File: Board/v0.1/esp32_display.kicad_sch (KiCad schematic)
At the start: 7 parts, among them J1 USB_B_Micro

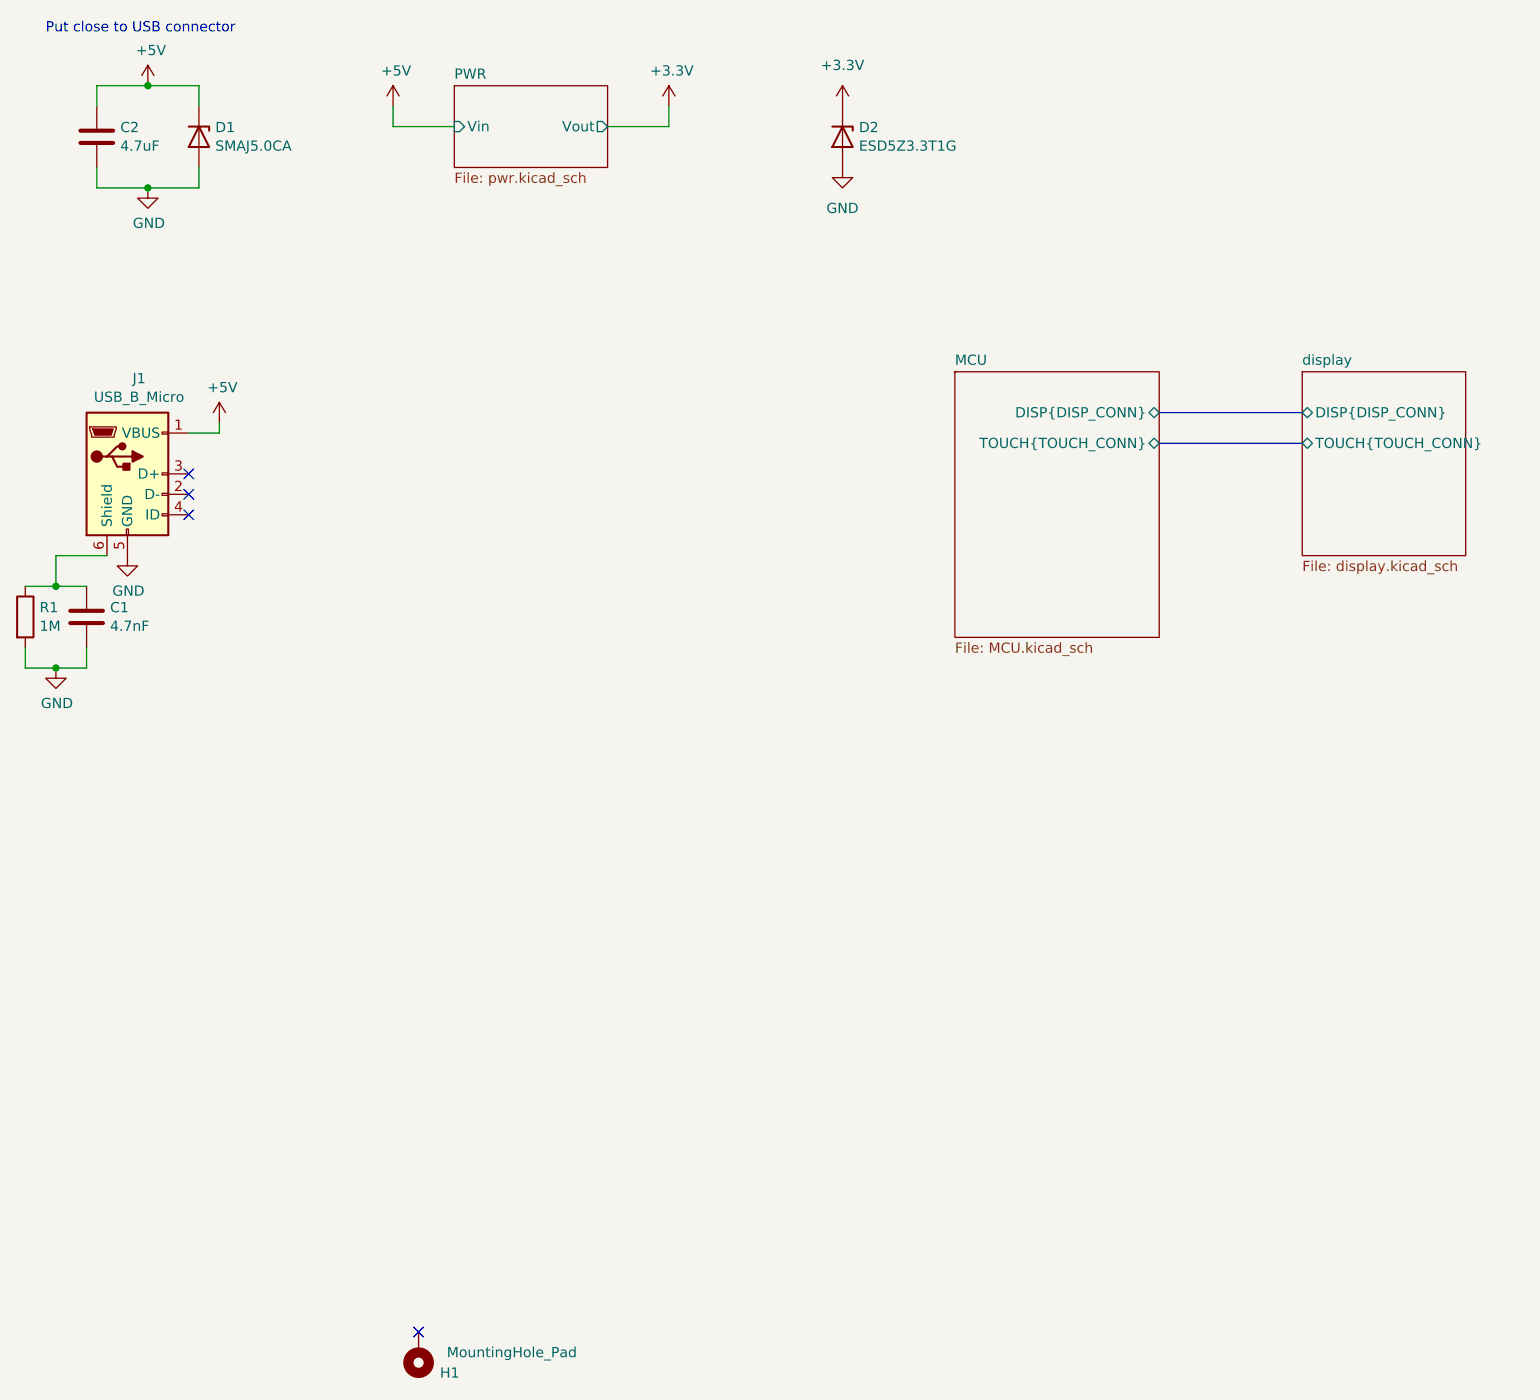
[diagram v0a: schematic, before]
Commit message: Clean schematics (add date and revision...)
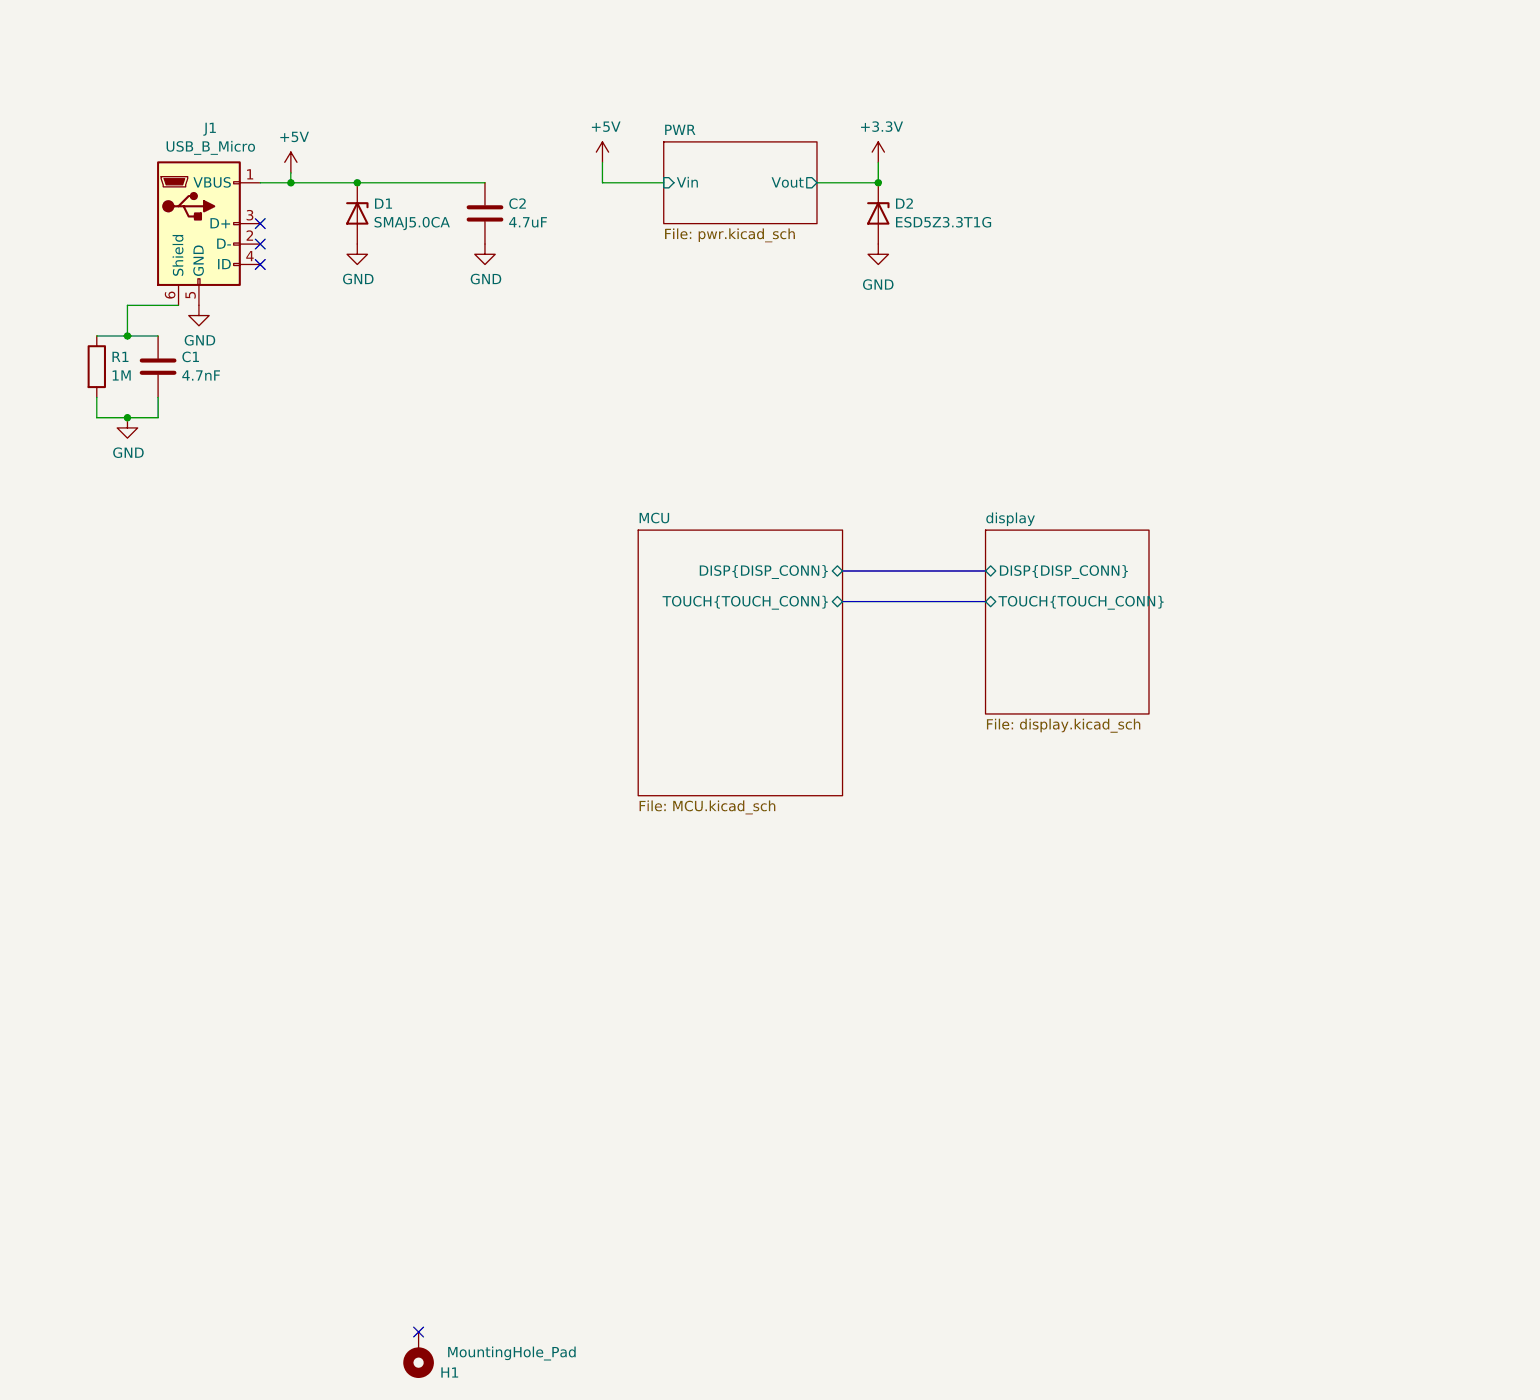
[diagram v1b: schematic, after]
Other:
- note removed: "Put close to USB connector"
- company: (none) -> Bzgec
- title: (none) -> ESP32_display
- moved on the sheet: C1, D2, J1, R1

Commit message: Add polyfuse, 3.3V status LED, USB_CONN sheet
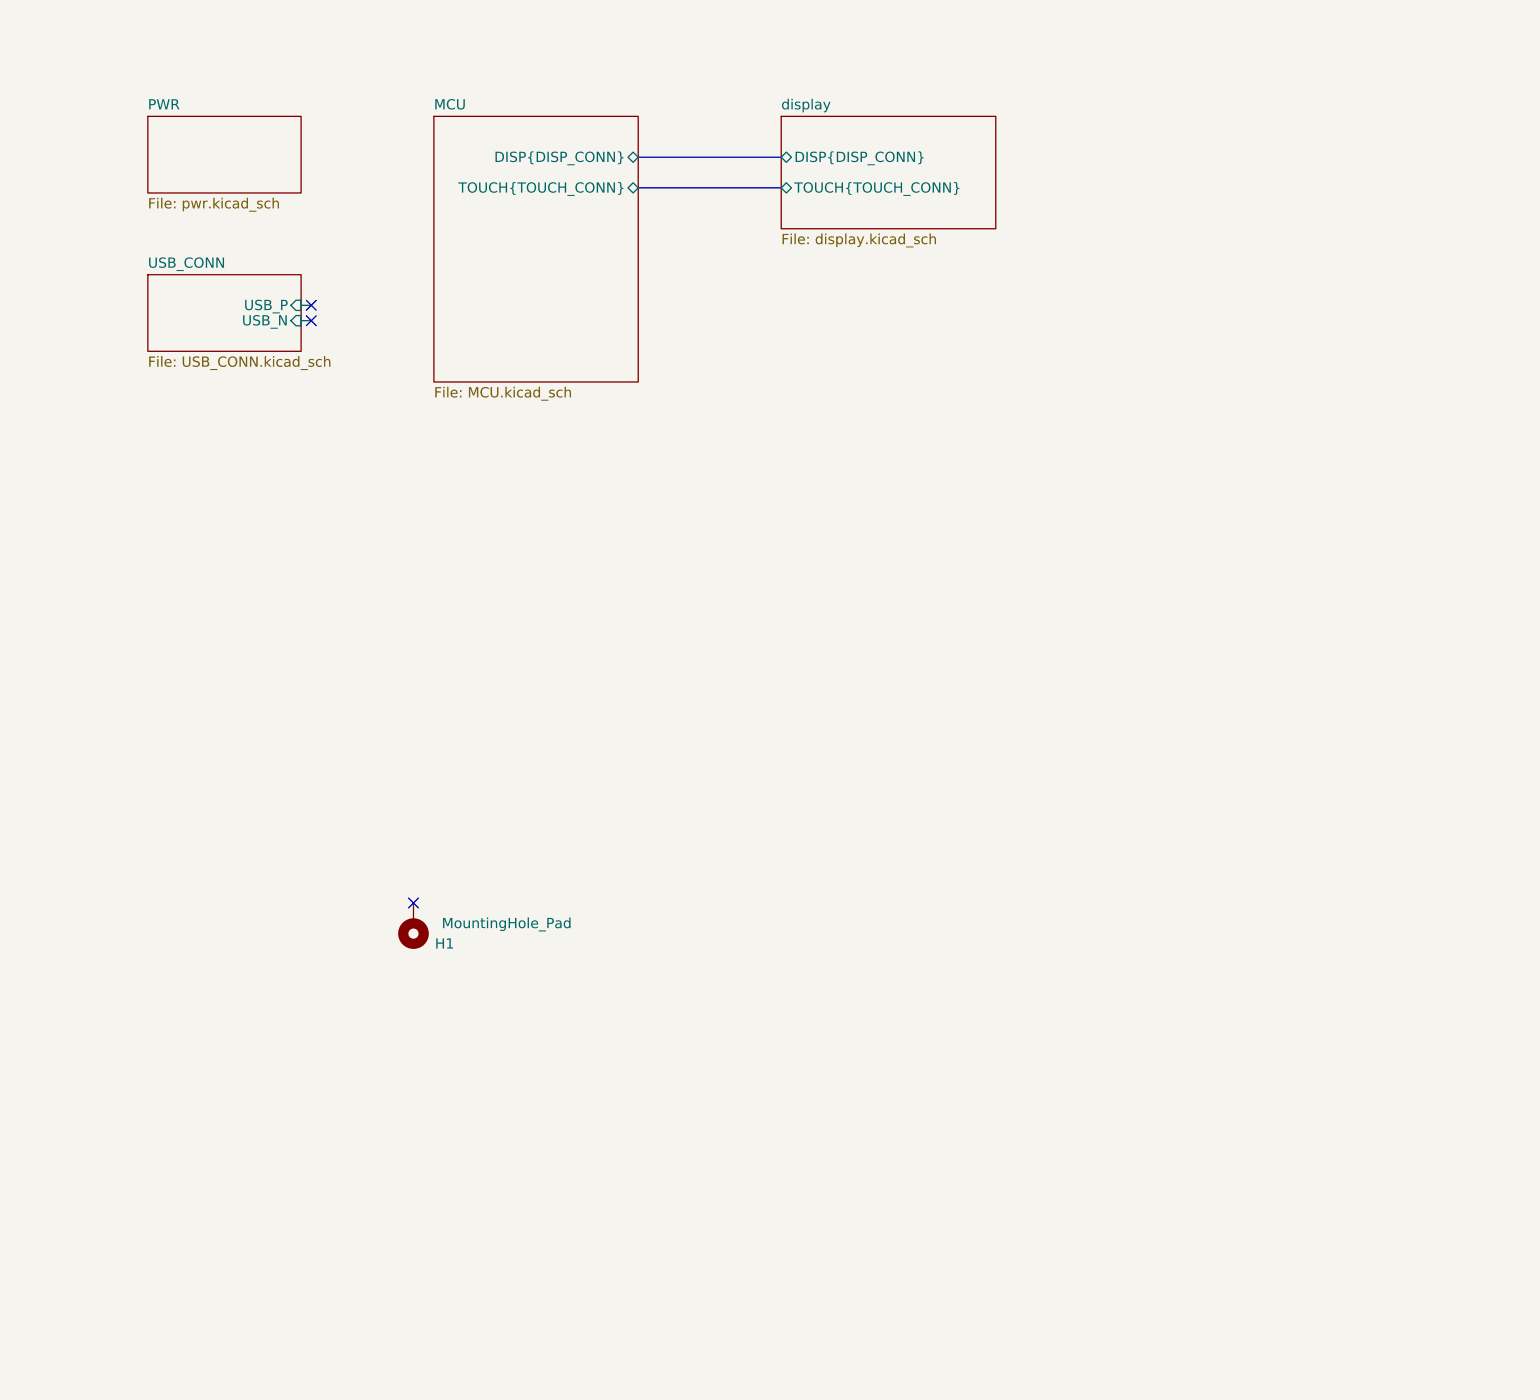
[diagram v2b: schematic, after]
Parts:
- removed C1: 4.7nF, Capacitor_SMD:C_0603_1608Metric_Pad1.08x0.95mm_HandSolder, symbol Device:C
- removed C2: 4.7uF, Capacitor_SMD:C_0603_1608Metric_Pad1.08x0.95mm_HandSolder, symbol Device:C
- removed D1: SMAJ5.0CA, Diode_SMD:D_SMA, symbol Device:D_Zener
- removed D2: ESD5Z3.3T1G, Diode_SMD:D_SOD-523, symbol Device:D_Zener
- removed J1: USB_B_Micro, myLib:USB_Micro-B_Molex-105017-0001, symbol Connector:USB_B_Micro
- removed R1: 1M, Resistor_SMD:R_0603_1608Metric_Pad0.98x0.95mm_HandSolder, symbol Device:R
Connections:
- no-connect marks 4 -> 3
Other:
- added sheet USB_CONN (USB_CONN.kicad_sch)
- sheet PWR ports: added none; removed Vin, Vout
- moved on the sheet: H1

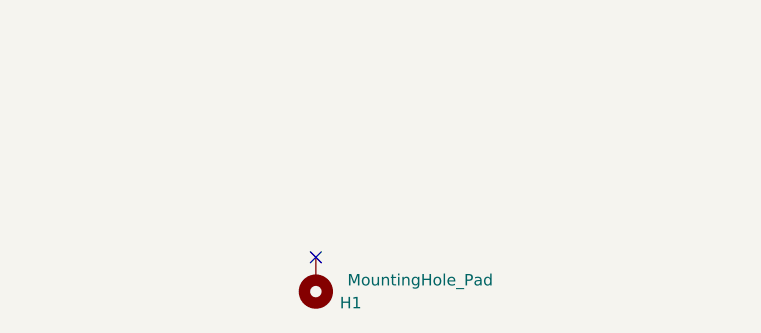
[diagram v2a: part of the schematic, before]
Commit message: Fix missing pad for H1, fix missing power input ERC error
ERC error was: Input power pin not driven by any output power pins.
Fix was adding PWR_FLAG power symbol after polyfuse or inductor.
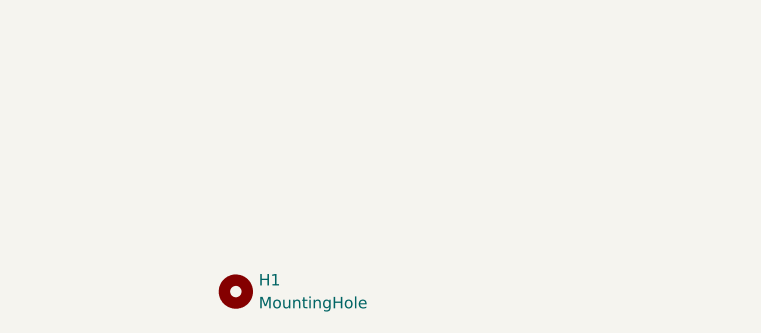
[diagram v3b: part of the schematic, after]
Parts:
- removed H1: MountingHole_Pad, MountingHole:MountingHole_3.2mm_M3_ISO14580, symbol Mechanical:MountingHole_Pad
- added H1: MountingHole, MountingHole:MountingHole_3.2mm_M3_ISO14580, symbol Mechanical:MountingHole
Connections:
- no-connect marks 3 -> 2
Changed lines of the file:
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@@
   (title_block
     (title "ESP32_display")
-    (date "2022/01/06")
+    (date "2022/01/07")
     (rev "v0.1")
     (company "Bzgec")
   )
-  (no_connect (at 67.31 124.46))
   (no_connect (at 54.61 52.07))
   (no_connect (at 54.61 50.165))
@@
     (stroke (width 0) (type default) (color 0 0 0 0))
   )
-  (symbol (lib_id "Mechanical:MountingHole_Pad") (at 67.31 127 180) (unit 1)
-    (in_bom yes) (on_board yes)
-    (property "Reference" "H1" (id 0) (at 72.39 129.54 0)
-      (effects (font (size 1.27 1.27)) (justify left))
-    )
-    (property "Value" "MountingHole_Pad" (id 1) (at 86.995 127 0)
-      (effects (font (size 1.27 1.27)) (justify left))
-    )
-    (property "Footprint" "MountingHole:MountingHole_3.2mm_M3_ISO14580" (id 2) (at 67.31 127 0)
+  (symbol (lib_id "Mechanical:MountingHole") (at 58.42 128.27 0) (unit 1)
+    (in_bom yes) (on_board yes) (fields_autoplaced)
+    (property "Reference" "H1" (id 0) (at 60.96 126.9999 0)
+      (effects (font (size 1.27 1.27)) (justify left))
+    )
+    (property "Value" "MountingHole" (id 1) (at 60.96 129.5399 0)
+      (effects (font (size 1.27 1.27)) (justify left))
+    )
+    (property "Footprint" "MountingHole:MountingHole_3.2mm_M3_ISO14580" (id 2) (at 58.42 128.27 0)
       (effects (font (size 1.27 1.27)) hide)
     )
-    (property "Datasheet" "~" (id 3) (at 67.31 127 0)
+    (property "Datasheet" "~" (id 3) (at 58.42 128.27 0)
       (effects (font (size 1.27 1.27)) hide)
     )
-    (pin "1")
   )
   (sheet (at 69.85 26.67) (size 25.4 33.02) (fields_autoplaced)
@@
   )
   (symbol_instances
+    (path "/00000000-0000-0000-0000-000061d02983/081a93ed-2bb5-4d25-aad0-5298afaf2352"
+      (reference "#FLG0101") (unit 1) (value "PWR_FLAG") (footprint "")
+    )
+    (path "/135735c6-9c20-4bf3-849f-8a3683d0618a/05b4fa5d-8a68-4d4c-9d29-1b03d8bf76d0"
+      (reference "#FLG0102") (unit 1) (value "PWR_FLAG") (footprint "")
+    )
     (path "/00000000-0000-0000-0000-000061c723b1/00000000-0000-0000-0000-000061d16a22"
       (reference "#PWR01") (unit 1) (value "GND") (footprint "")
@@
       (reference "F1") (unit 1) (value "500mA, 1A") (footprint "Fuse:Fuse_1206_3216Metric_Pad1.42x1.75mm_HandSolder")
     )
-    (path "/52c72b0a-7b13-4e4f-b408-f755e8ea0b56"
-      (reference "H1") (unit 1) (value "MountingHole_Pad") (footprint "MountingHole:MountingHole_3.2mm_M3_ISO14580")
+    (path "/e6cd0f10-9fef-46a7-a969-4cb23dfea13f"
+      (reference "H1") (unit 1) (value "MountingHole") (footprint "MountingHole:MountingHole_3.2mm_M3_ISO14580")
     )
     (path "/00000000-0000-0000-0000-000061c723b1/785bf931-de50-44b9-a6a1-eebb5527f4a4"

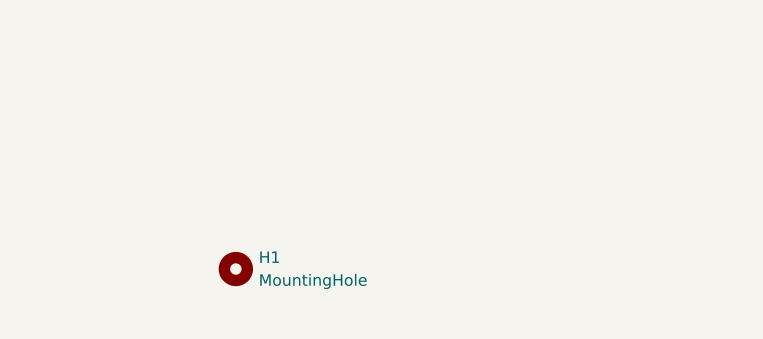
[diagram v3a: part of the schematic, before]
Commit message: Generate gerbers, sch and BOM with KiBot
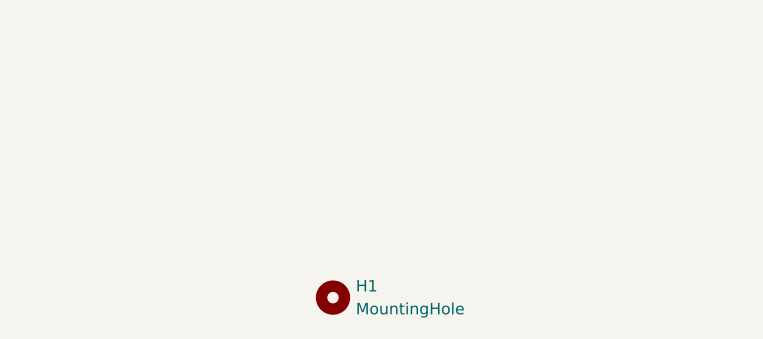
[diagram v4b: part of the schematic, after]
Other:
- moved on the sheet: H1
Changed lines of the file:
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@@
     (stroke (width 0) (type default) (color 0 0 0 0))
   )
-  (symbol (lib_id "Mechanical:MountingHole") (at 58.42 128.27 0) (unit 1)
+  (symbol (lib_id "Mechanical:MountingHole") (at 69.215 131.445 0) (unit 1)
     (in_bom yes) (on_board yes) (fields_autoplaced)
-    (property "Reference" "H1" (id 0) (at 60.96 126.9999 0)
+    (property "Reference" "H1" (id 0) (at 71.755 130.1749 0)
       (effects (font (size 1.27 1.27)) (justify left))
     )
-    (property "Value" "MountingHole" (id 1) (at 60.96 129.5399 0)
+    (property "Value" "MountingHole" (id 1) (at 71.755 132.7149 0)
       (effects (font (size 1.27 1.27)) (justify left))
     )
-    (property "Footprint" "MountingHole:MountingHole_3.2mm_M3_ISO14580" (id 2) (at 58.42 128.27 0)
+    (property "Footprint" "MountingHole:MountingHole_3.2mm_M3_ISO14580" (id 2) (at 69.215 131.445 0)
       (effects (font (size 1.27 1.27)) hide)
     )
-    (property "Datasheet" "~" (id 3) (at 58.42 128.27 0)
+    (property "Datasheet" "~" (id 3) (at 69.215 131.445 0)
       (effects (font (size 1.27 1.27)) hide)
     )
@@
   (symbol_instances
     (path "/00000000-0000-0000-0000-000061d02983/081a93ed-2bb5-4d25-aad0-5298afaf2352"
-      (reference "#FLG0101") (unit 1) (value "PWR_FLAG") (footprint "")
+      (reference "#FLG01") (unit 1) (value "PWR_FLAG") (footprint "")
     )
     (path "/135735c6-9c20-4bf3-849f-8a3683d0618a/05b4fa5d-8a68-4d4c-9d29-1b03d8bf76d0"
-      (reference "#FLG0102") (unit 1) (value "PWR_FLAG") (footprint "")
+      (reference "#FLG02") (unit 1) (value "PWR_FLAG") (footprint "")
     )
     (path "/00000000-0000-0000-0000-000061c723b1/00000000-0000-0000-0000-000061d16a22"
